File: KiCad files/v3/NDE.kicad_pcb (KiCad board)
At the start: 2 copper layers, 90 x 90 mm, 27 parts, among them J1 Nabíjací modul, J10 Conn_01x01_Socket, J11 Conn_01x01_Socket, J12 Conn_01x01_Socket, J13 Conn_01x01_Socket, J14 VM_Select, J2 Step-up input, J3 Step-up output, J6 Conn_01x05_Socket, J7 Conn_01x08_Socket, J8 Conn_01x20_Socket, J9 Conn_01x20_Socket, U1 LM7805_TO220

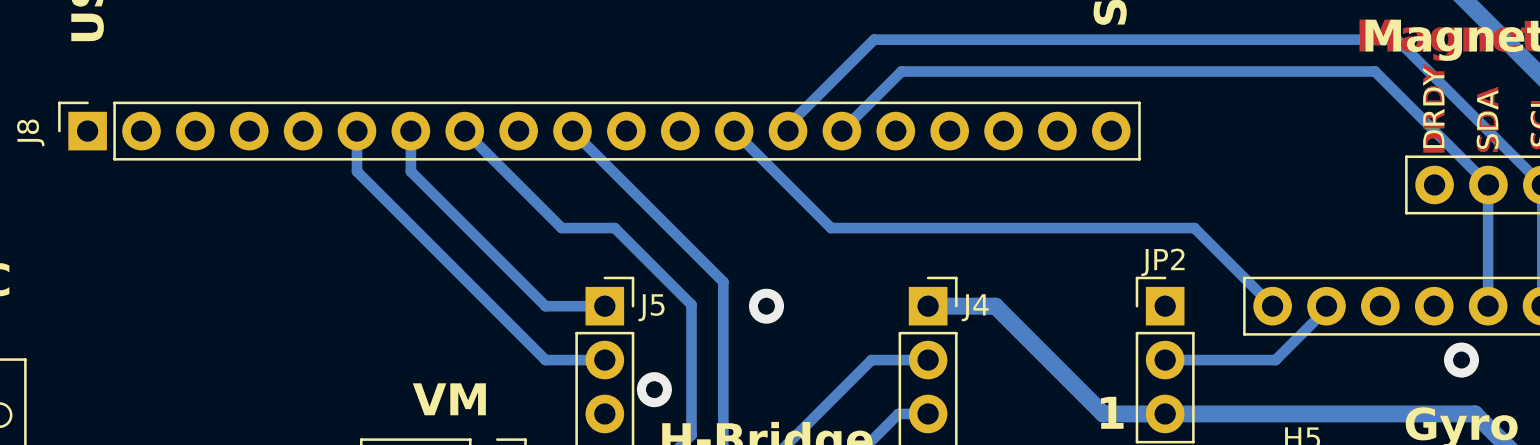
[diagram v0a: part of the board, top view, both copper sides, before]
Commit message: Identified footprint issue - needs fixing
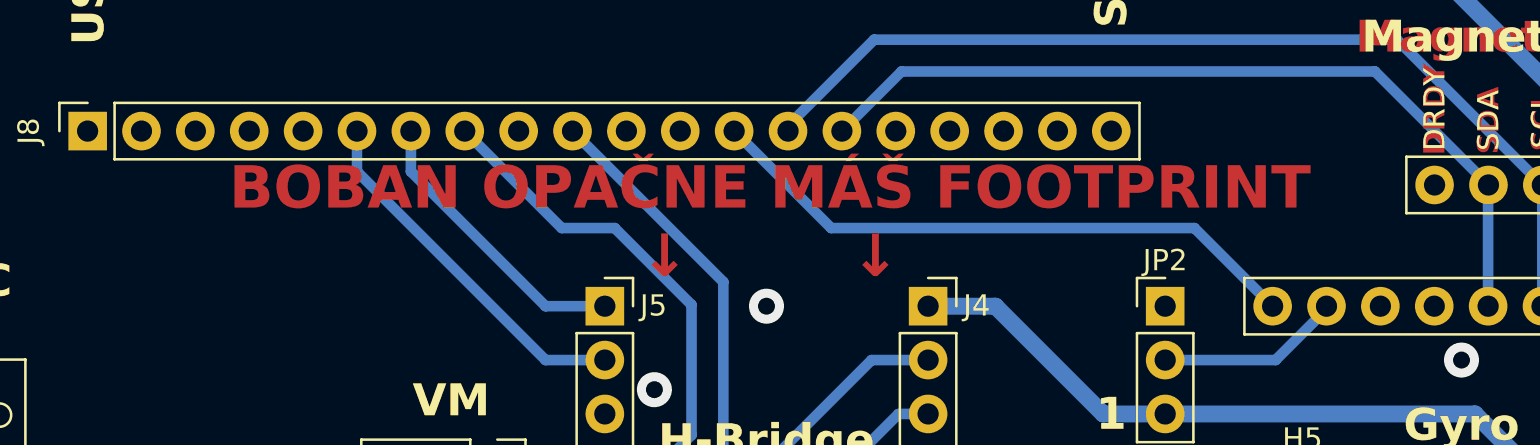
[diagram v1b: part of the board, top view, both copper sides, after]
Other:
- board text added: "BOBAN OPAČNE MÁŠ FOOTPRINT ↓ ↓"
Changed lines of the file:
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@@
+		)
+	)
+	(gr_text "BOBAN OPAČNE MÁŠ FOOTPRINT\n↓		↓"
+		(at 145.2 71.6 0)
+		(layer "F.Cu" knockout)
+		(effects
+			(font
+				(size 2 2)
+				(thickness 0.4)
+				(bold yes)
+			)
 		)
 	)
